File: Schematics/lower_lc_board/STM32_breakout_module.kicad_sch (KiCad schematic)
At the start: 44 parts, among them J2 SWD_CONN, J3 USB_C_CONN, SW1 SW_STM_RESET, SW2 SW_STM_BOOT_MODE, U5 STM32F103CBT6, U6 W25Q128JVS, U7 ISO1044BDR, U8 CP2102N-Axx-xQFN20, Y1 X322516MMB4SI

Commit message: updates and added to cart
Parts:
- removed C18, C19, C22: 0.1uF, Capacitor_SMD:C_0603_1608Metric, symbol Device:C
- removed R16: 470, Resistor_SMD:R_0603_1608Metric, symbol Device:R
- removed U7: ISO1044BDR, ul_ISO1044BDR:SOIC_1044BDR_TEX, symbol Interface_CAN_LIN:ISO1044BD
- added C8: 100nF, Capacitor_SMD:C_0603_1608Metric, symbol Device:C
- added R46: 120, Resistor_SMD:R_0603_1608Metric, symbol Device:R
- added U1: TCAN1051HGVDR, ul_ISO1044BDR:SOIC_1044BDR_TEX, symbol Interface_CAN_LIN:TCAN330
- FB2: value 100R -> 600R; LCSC 1002 -> C1002
- R60: value 100k -> 10k
- U6: value W25Q128JVS -> BY25Q128ES; Digikey (none) -> 5369-BY25Q128ESSIG(R)CT-ND; LCSC C97521 -> (none)
- U8: footprint CP2102N_A02_GQFN20:QFN20_CP2102N_SIL -> digikey-footprints:QFN-20-1EP_3x3mm
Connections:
- net +3V3: now also SW2.2; no longer SW2.1
- net +5V: now also C9.2, U1.3 (VCC)
- net BOOT0: now also SW2.1; no longer SW2.2
- net CAN_LED: now also U5.40 (PB4); no longer U5.19 (PB1)
- net CAN_N: now also R46.1, U1.6 (CANL)
- net CAN_P: now also R46.2, U1.7 (CANH)
- net CAN_RX: now also U1.4 (RXD)
- net CAN_TX: now also U1.1 (TXD)
- net GND: now also C8.2, U1.2 (GND)
- net RGB_DATA: now also D7.4 (DIN)
- net STM_RESET: now also C8.1; no longer C9.2
- new net VSOL_SENSE: U5.19 (PB1)
- no-connect marks 19 -> 20
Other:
- note added: "B0 HIGH = PROGRAMMING MODE B0 LOW = RUN MEMORY"
- note added: "CANbus termination"
- note added: "NOTE: Not typtical CANT used, ISO1044BDR was out of stock"
- note added: "NOTE: Not typtical flash used, pins are identical but lower write speeds"
- note removed: "* needs software remap"
- note removed: "active-high"
- note removed: "place near RGBLED_VDD pin for local decoupling"
- title: HYDRA | STM32 Breakout Circuitry -> STM32 Breakout Circuitry
- moved on the sheet: C16, C20, C21, D5, D6, D7, R11, R12, R13, R14, R15, R48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

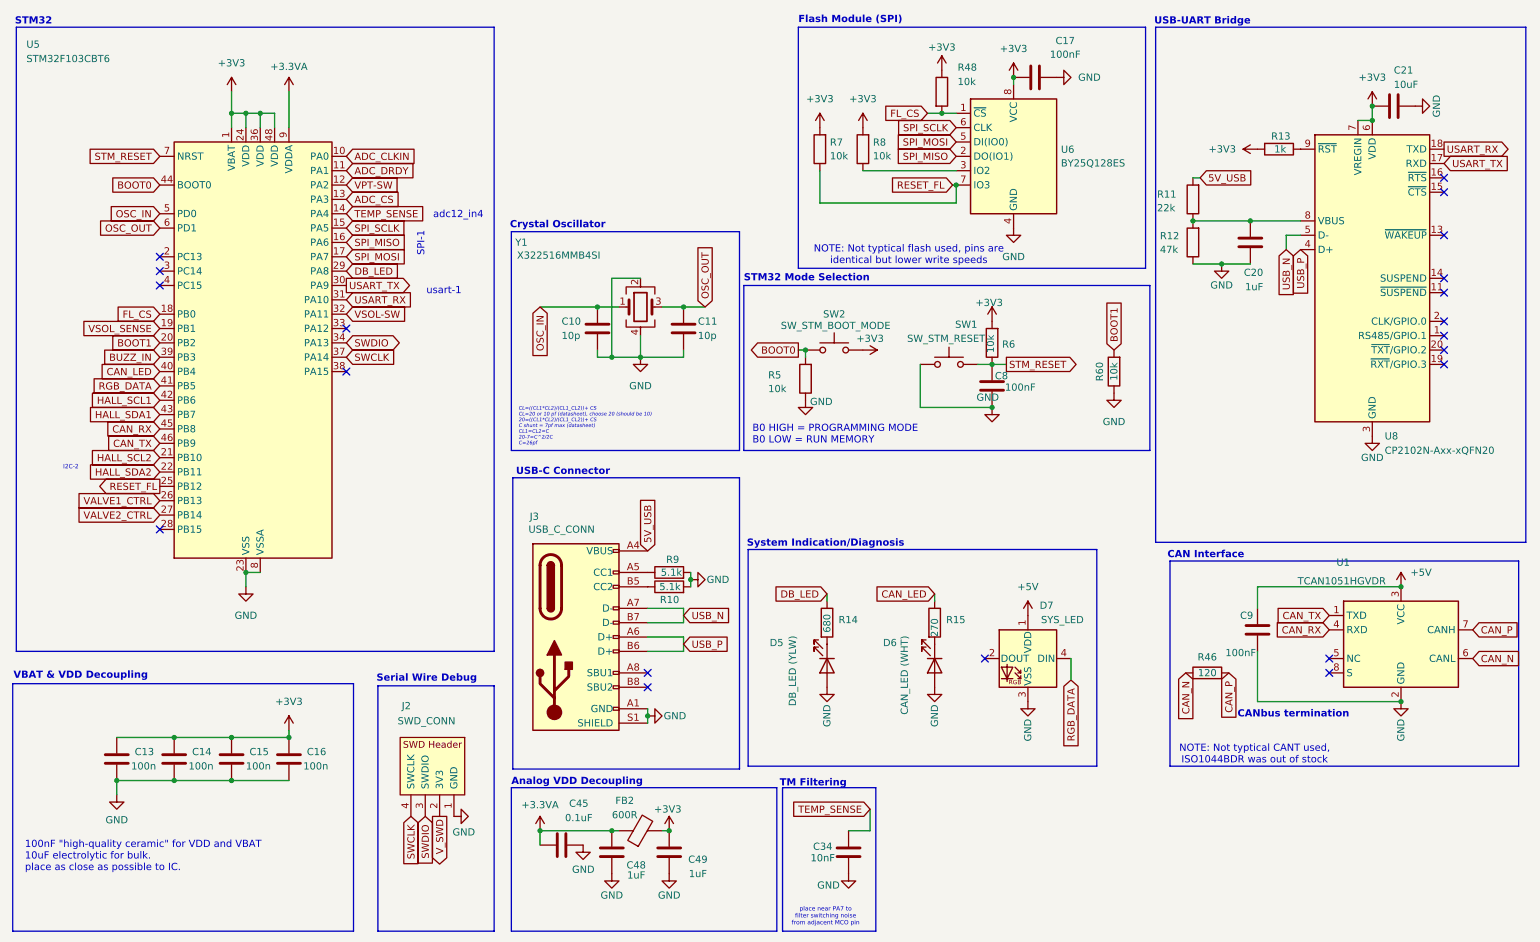
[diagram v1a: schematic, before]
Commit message: add board-specifc READMEs (TODO), cleanup schematic titles
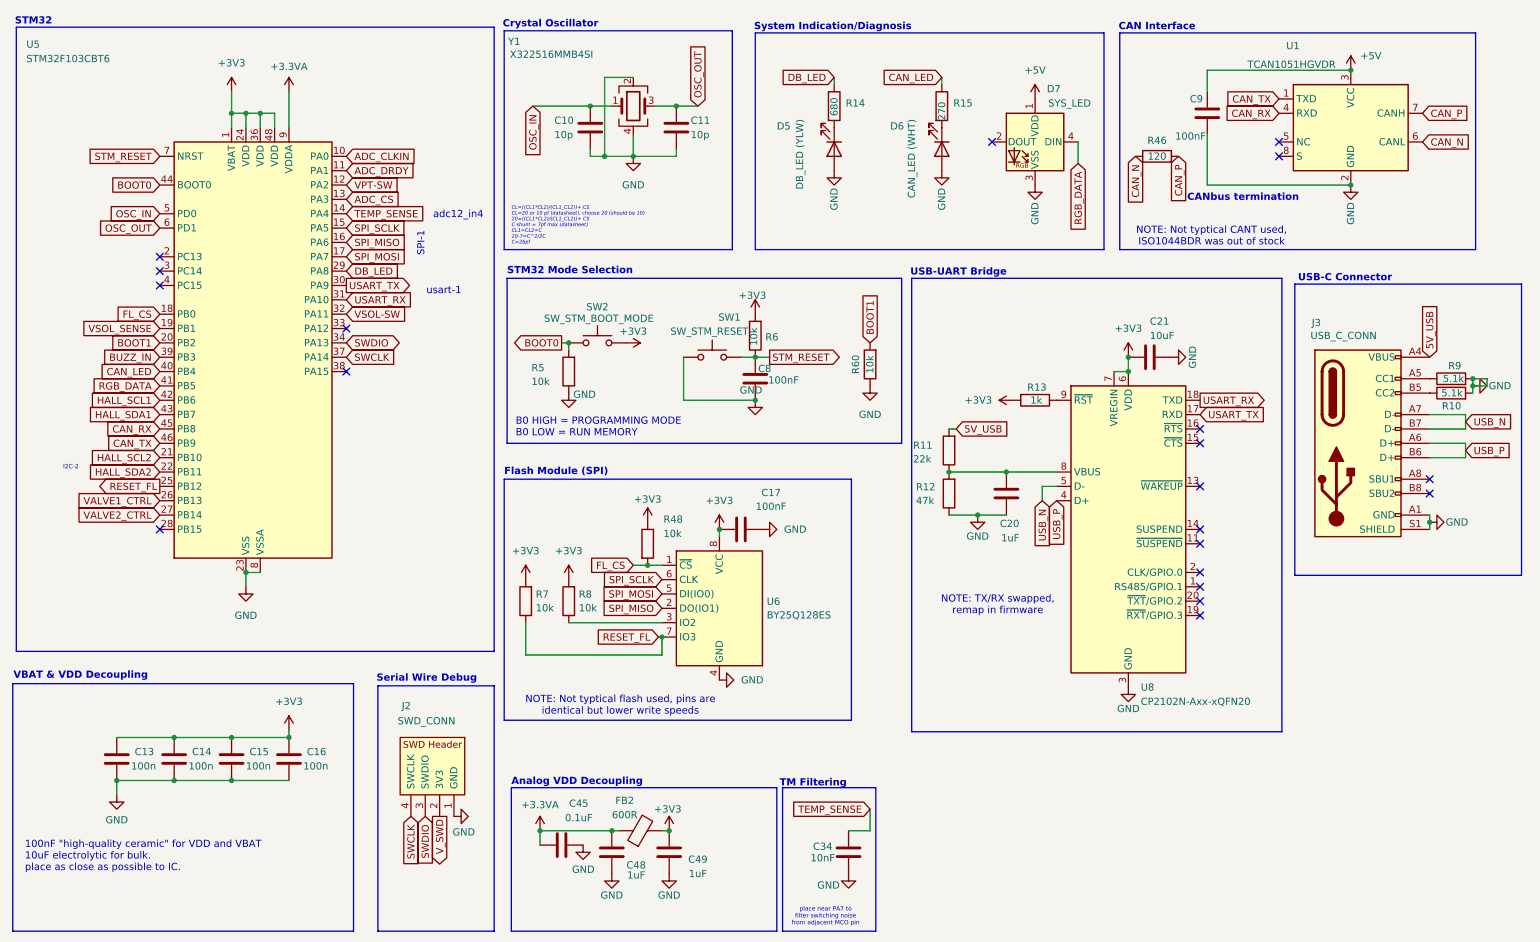
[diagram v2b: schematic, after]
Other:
- note added: "NOTE: TX/RX swapped, remap in firmware"
- moved on the sheet: C10, C11, C17, C20, C21, C8, C9, D5, D6, D7, J3, R10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

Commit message: add ed pinouts
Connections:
- net BUZZ_IN: no longer names the net of U5.39 (PB3)
- net TEMP_SENSE renamed CJC_SENSE
- net VALVE1_CTRL renamed SOL1_EN
- net VALVE2_CTRL renamed SOL2_EN
- net VPT-SW renamed VPT_EN
- net VSOL-SW renamed VSOL_EN
- no-connect marks 20 -> 21
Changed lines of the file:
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@@
+	)
+	(no_connect
+		(at 41.91 83.82)
 	)
 	(no_connect
@@
 		)
 	)
-	(global_label "TEMP_SENSE"
+	(global_label "CJC_SENSE"
 		(shape input)
 		(at 167.64 163.83 180)
@@
 		)
 		(property "Intersheetrefs" "${INTERSHEET_REFS}"
-			(at 152.8017 163.83 0)
+			(at 154.1321 163.83 0)
 			(effects
 				(font
@@
 		)
 	)
-	(global_label "VSOL-SW"
+	(global_label "VSOL_EN"
 		(shape input)
 		(at 74.93 76.2 0)
@@
 		)
 		(property "Intersheetrefs" "${INTERSHEET_REFS}"
-			(at 86.8052 76.2 0)
+			(at 86.019 76.2 0)
 			(effects
 				(font
@@
 		)
 	)
-	(global_label "TEMP_SENSE"
+	(global_label "CJC_SENSE"
 		(shape input)
 		(at 74.93 58.42 0)
@@
 		)
 		(property "Intersheetrefs" "${INTERSHEET_REFS}"
-			(at 89.7683 58.42 0)
+			(at 88.4379 58.42 0)
 			(effects
 				(font
@@
 		)
 	)
-	(global_label "VPT-SW"
+	(global_label "VPT_EN"
 		(shape input)
 		(at 74.93 53.34 0)
@@
 		)
 		(property "Intersheetrefs" "${INTERSHEET_REFS}"
-			(at 85.4747 53.34 0)
+			(at 84.6885 53.34 0)
 			(effects
 				(font
@@
 		)
 	)
-	(global_label "VALVE2_CTRL"
+	(global_label "SOL2_EN"
 		(shape input)
 		(at 41.91 111.76 180)
@@
 		)
 		(property "Intersheetrefs" "${INTERSHEET_REFS}"
-			(at 26.7691 111.76 0)
+			(at 30.7001 111.76 0)
 			(effects
 				(font
@@
 		)
 	)
-	(global_label "BUZZ_IN"
-		(shape input)
-		(at 41.91 83.82 180)
-		(fields_autoplaced yes)
-		(effects
-			(font
-				(size 1.27 1.27)
-			)
-			(justify right)
-		)
-		(property "Intersheetrefs" "${INTERSHEET_REFS}"
-			(at 31.0024 83.82 0)
-			(effects
-				(font
-					(size 1.27 1.27)
-				)
-				(justify right)
-				(hide yes)
-			)
-		)
-	)
 	(global_label "HALL_SDA1"
 		(shape input)
@@
 		)
 	)
-	(global_label "VALVE1_CTRL"
+	(global_label "SOL1_EN"
 		(shape input)
 		(at 41.91 109.22 180)
@@
 		)
 		(property "Intersheetrefs" "${INTERSHEET_REFS}"
-			(at 26.7691 109.22 0)
-			(effects
-				(font
+			(at 30.7001 109.22 0)
+			(effects
+				(font
